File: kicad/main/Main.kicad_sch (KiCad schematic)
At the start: 0 parts

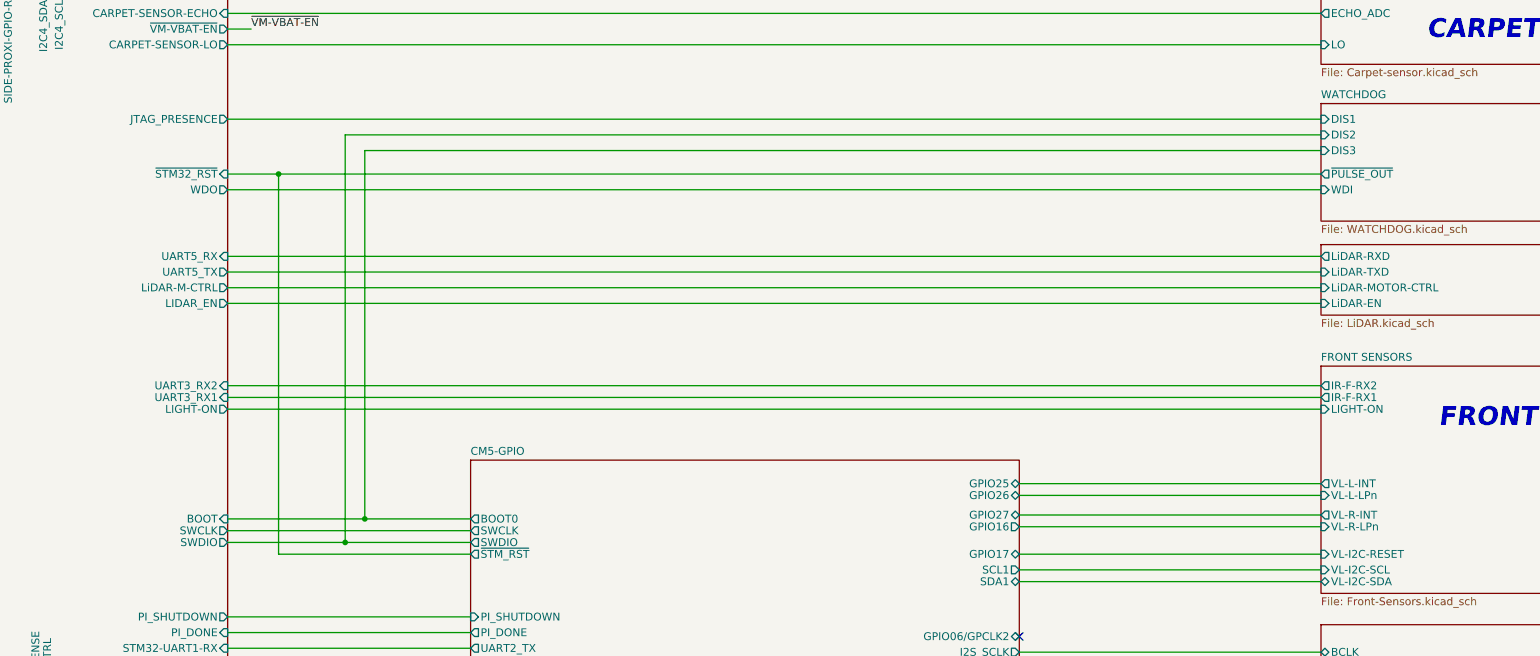
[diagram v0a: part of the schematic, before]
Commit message: Cleanup; renamed WDO to WDI
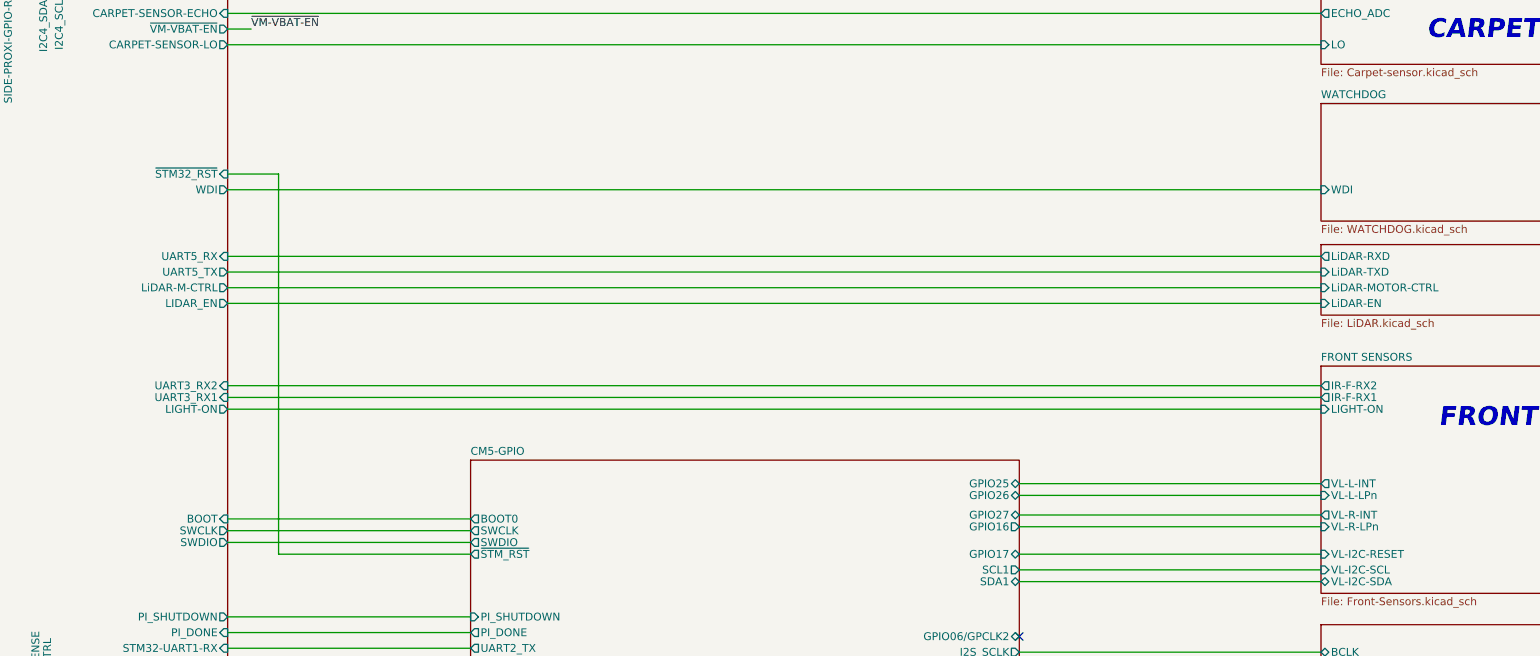
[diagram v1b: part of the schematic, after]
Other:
- sheet MCU-STM32 ports: added WDI; removed JTAG_PRESENCE, WDO
- sheet WATCHDOG ports: added none; removed DIS1, DIS2, DIS3, ~{PULSE_OUT}
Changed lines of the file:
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@@
 		)
 	)
-	(junction
-		(at 288.925 200.025)
-		(diameter 0)
-		(color 0 0 0 0)
-	)
-	(junction
-		(at 285.75 203.835)
-		(diameter 0)
-		(color 0 0 0 0)
-	)
-	(junction
-		(at 274.955 144.145)
-		(diameter 0)
-		(color 0 0 0 0)
-	)
 	(no_connect
 		(at 394.97 219.075)
@@
 	(wire
 		(pts
-			(xy 285.75 203.835) (xy 285.75 137.795)
-		)
-		(stroke
-			(width 0)
-			(type default)
-		)
-	)
-	(wire
-		(pts
 			(xy 394.97 226.695) (xy 443.865 226.695)
 		)
@@
 	(wire
 		(pts
-			(xy 274.955 144.145) (xy 443.865 144.145)
-		)
-		(stroke
-			(width 0)
-			(type default)
-		)
-	)
-	(wire
-		(pts
-			(xy 288.925 200.025) (xy 288.925 140.335)
-		)
-		(stroke
-			(width 0)
-			(type default)
-		)
-	)
-	(wire
-		(pts
 			(xy 394.97 347.98) (xy 443.865 347.98)
 		)
@@
 	(wire
 		(pts
-			(xy 285.75 203.835) (xy 306.07 203.835)
-		)
-		(stroke
-			(width 0)
-			(type default)
-		)
-	)
-	(wire
-		(pts
 			(xy 394.97 317.5) (xy 443.865 317.5)
 		)
@@
 	(wire
 		(pts
-			(xy 266.7 135.255) (xy 443.865 135.255)
-		)
-		(stroke
-			(width 0)
-			(type default)
-		)
-	)
-	(wire
-		(pts
 			(xy 220.345 234.315) (xy 220.345 346.71)
 		)
@@
 	(wire
 		(pts
-			(xy 285.75 137.795) (xy 443.865 137.795)
-		)
-		(stroke
-			(width 0)
-			(type default)
-		)
-	)
-	(wire
-		(pts
 			(xy 394.97 313.055) (xy 443.865 313.055)
 		)
@@
 	(wire
 		(pts
-			(xy 266.7 203.835) (xy 285.75 203.835)
+			(xy 266.7 203.835) (xy 306.07 203.835)
 		)
 		(stroke
@@
 	(wire
 		(pts
-			(xy 288.925 200.025) (xy 306.07 200.025)
-		)
-		(stroke
-			(width 0)
-			(type default)
-		)
-	)
-	(wire
-		(pts
 			(xy 196.215 57.785) (xy 179.07 57.785)
 		)
@@
 	(wire
 		(pts
-			(xy 288.925 140.335) (xy 443.865 140.335)
-		)
-		(stroke
-			(width 0)
-			(type default)
-		)
-	)
-	(wire
-		(pts
 			(xy 394.97 332.74) (xy 443.865 332.74)
 		)
@@
 	(wire
 		(pts
-			(xy 266.7 200.025) (xy 288.925 200.025)
+			(xy 266.7 200.025) (xy 306.07 200.025)
 		)
 		(stroke
@@
 			)
 		)
-		(pin "WDO" output
+		(pin "WDI" output
 			(at 266.7 146.685 0)
 			(effects
@@
 			)
 		)
-		(pin "JTAG_PRESENCE" output
-			(at 266.7 135.255 0)
-			(effects
-				(font
-					(size 1.27 1.27)
-				)
-				(justify right)
-			)
-		)
 		(instances
 			(project "Main"
@@
 		)
 		(fill
-			(color 128 255 128 1)
+			(color 0 72 0 1)
 		)
 		(property "Sheetname" "WATCHDOG"
@@
 			(effects
 				(font
-					(size 1.27 1.27)
-				)
-				(justify left)
-			)
-		)
-		(pin "~{PULSE_OUT}" output
-			(at 443.865 144.145 180)
-			(effects
-				(font
-					(size 1.27 1.27)
-				)
-				(justify left)
-			)
-		)
-		(pin "DIS1" input
-			(at 443.865 135.255 180)
-			(effects
-				(font
-					(size 1.27 1.27)
-				)
-				(justify left)
-			)
-		)
-		(pin "DIS2" input
-			(at 443.865 137.795 180)
-			(effects
-				(font
-					(size 1.27 1.27)
-				)
-				(justify left)
-			)
-		)
-		(pin "DIS3" input
-			(at 443.865 140.335 180)
-			(effects
-				(font
